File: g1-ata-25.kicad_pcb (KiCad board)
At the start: 2 copper layers, 29 parts, among them P1 G1_DC_SOCKET, P2 G1_GD_PLUGNH, P3 IDE_40PIN, P4 IDE_44PIN, P5 CONN_01X02, P6 CONN_01X04, P7 BARREL_JACK, P8 CONN_01X05, U1 TCXO_DFAS11, U2 TS30011-M050

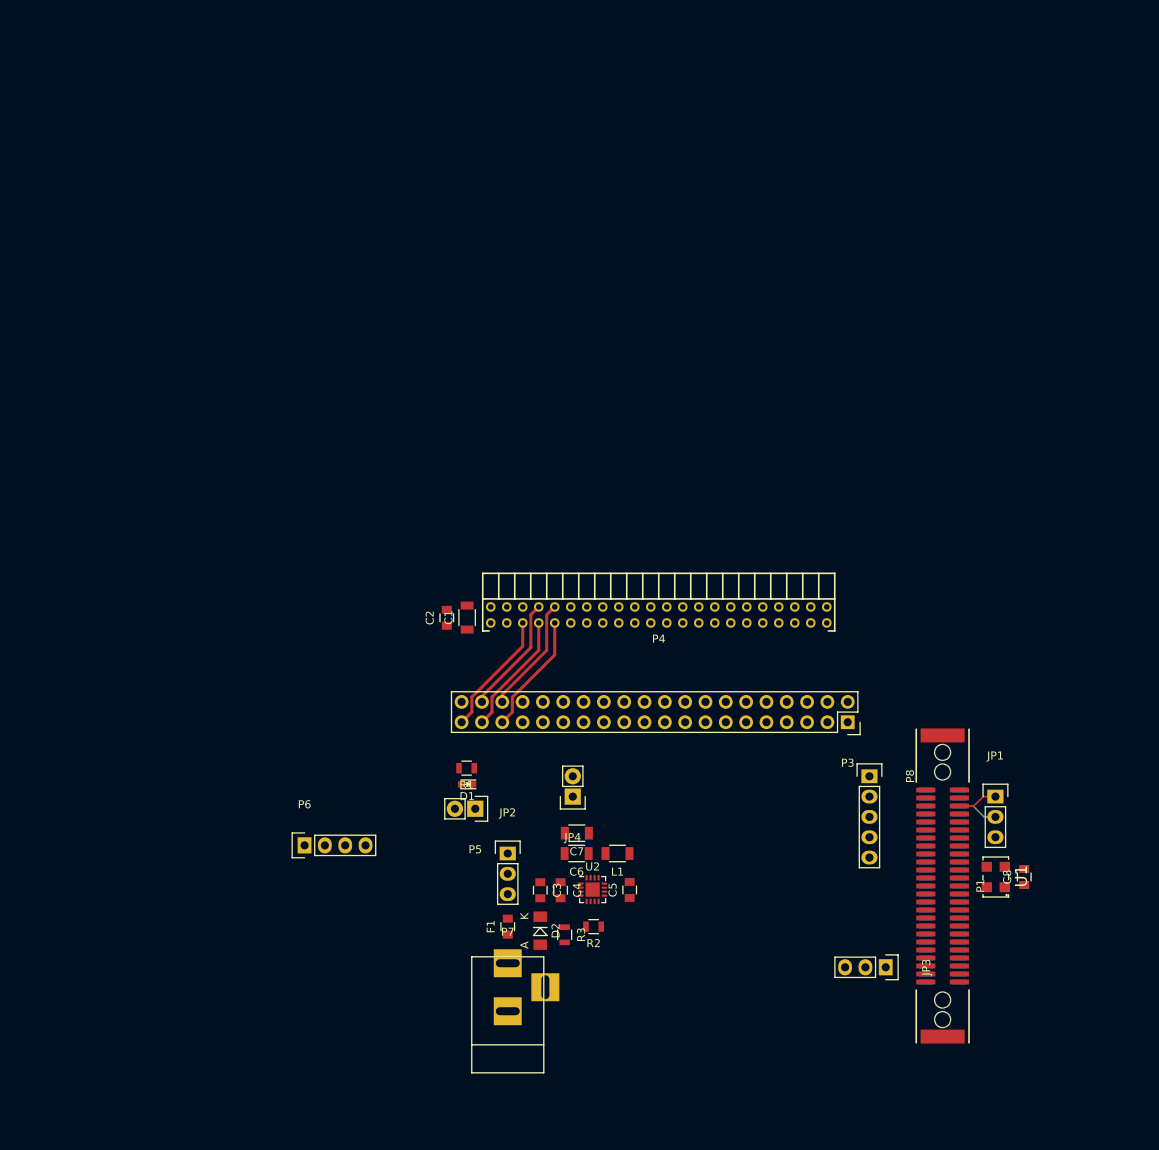
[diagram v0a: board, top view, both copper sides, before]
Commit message: Moved some components.
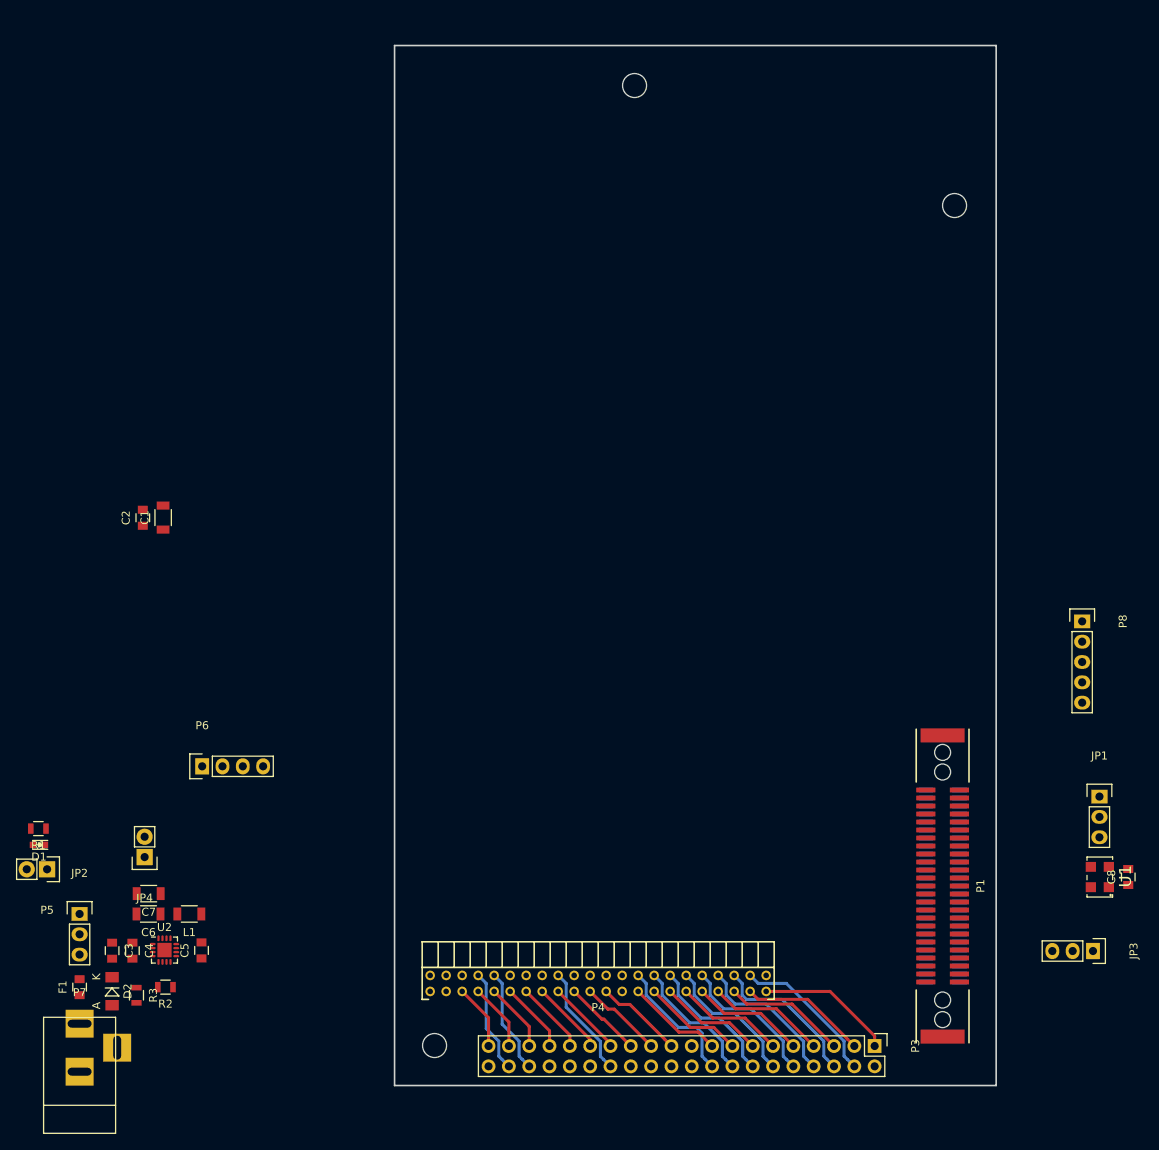
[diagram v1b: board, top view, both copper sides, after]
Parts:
- added MountingHole_3mm: VAL**, Mounting_Holes:MountingHole_3mm, F.Cu at (155.6, 24.4)
- added MountingHole_3mm: VAL**, Mounting_Holes:MountingHole_3mm, F.Cu at (195.6, 39.4)
- added MountingHole_3mm: VAL**, Mounting_Holes:MountingHole_3mm, F.Cu at (130.6, 144.4)
- P3: footprint Socket_Strips:Socket_Strip_Straight_2x20 -> Pin_Headers:Pin_Header_Straight_2x20
- moved C7 54.1 mm to (94.8, 125.4)
- moved C3 54.1 mm to (90.2, 132.5)
- moved C4 54.1 mm to (92.8, 132.5)
- moved C6 54.1 mm to (94.8, 128.0)
- moved D1 54.1 mm to (81.1, 119.3)
- moved D2 54.1 mm to (90.2, 137.6)
- moved JP4 54.1 mm to (94.3, 120.8)
- moved R1 54.1 mm to (81.0, 117.3)
- moved R3 54.1 mm to (93.3, 138.1)
- moved U2 54.1 mm to (96.8, 132.5)
- moved C5 54.1 mm to (101.4, 132.5)
- moved F1 54.1 mm to (86.2, 137.1)
- moved JP2 54.1 mm to (86.2, 128.0)
- moved L1 54.1 mm to (99.9, 128.0)
- moved P5 54.1 mm to (82.1, 122.4)
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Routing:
- net /DD9: track 0.00 -> 19.1 mm
- net /DD8: track 0.00 -> 18.8 mm
- net /DD10: track 0.00 -> 18.6 mm
- net /DD11: track 0.00 -> 18.1 mm
- net /DD12: track 0.00 -> 17.5 mm
- net /~GDD_RST: track 0.00 -> 17.1 mm
- net /DD13: track 0.00 -> 17.0 mm
- net /DD15: track 0.00 -> 16.5 mm
- net /DD14: track 0.00 -> 16.4 mm
- net /DD7: track 0.00 -> 15.8 mm
- net /DD6: track 0.00 -> 15.3 mm
- net /DD5: track 0.00 -> 14.8 mm
- net /DD4: track 0.00 -> 14.2 mm
- net /CSEL: track 0.00 -> 14.1 mm
- net /DD3: track 0.00 -> 13.7 mm
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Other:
- board outline added: 75.2 x 130 mm
- board text added: "10.65"
- board text added: "6.7"

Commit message: Routing...
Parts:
- P7: value BARREL_JACK -> CONN_01X02; footprint Connect:BARREL_JACK -> Sockets_WAGO734:WAGO_734_2pin_Straight_RuggedPads
- moved R3 153.6 mm to (194.3, 22.4), turned to 0 degrees
- moved C3 151.0 mm to (197.9, 26.7), turned to 90 degrees
- moved R2 148.4 mm to (191.0, 22.4), turned to 0 degrees
- moved C4 147.6 mm to (195.6, 26.7), turned to 90 degrees
- moved U2 141.7 mm to (191.3, 26.8), turned to 180 degrees
- moved P7 140.6 mm to (195.3, 59.2), turned to 270 degrees
- moved F1 138.4 mm to (195.8, 52.6), turned to 0 degrees
- moved C6 138.0 mm to (193.3, 31.4), turned to 0 degrees
- moved D2 137.0 mm to (195.6, 50.0), turned to 180 degrees
- moved C5 135.9 mm to (186.9, 26.9), turned to 270 degrees
- moved C7 134.4 mm to (193.2, 33.9), turned to 0 degrees
- moved JP2 134.2 mm to (192.8, 46.5), turned to 90 degrees
- moved L1 130.9 mm to (188.2, 31.4), turned to 0 degrees
- moved JP3 114.9 mm to (182.4, 21.8), turned to 0 degrees
- moved P5 112.1 mm to (134.6, 23.4)
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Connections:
- P8 pad 1: /CD_LRCK -> /~CD_LRCK
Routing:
- net +5V: track 0.00 -> 178.1 mm
- net +5VP: track 0.00 -> 129.4 mm, vias 0 -> 2
- net /CSEL: track 14.1 -> 126.5 mm, vias 0 -> 1
- net /~ACTIVE: track 8.19 -> 117.7 mm
- net /IORDY: track 9.53 -> 111.4 mm, vias 0 -> 2
- net /INTRQ: track 9.09 -> 109.2 mm, vias 0 -> 2
- net /DA1: track 8.86 -> 107.3 mm, vias 0 -> 2
- net /DA2: track 13.2 -> 107.7 mm, vias 0 -> 2
- net /~IDE_CS1: track 13.0 -> 96.5 mm, vias 0 -> 1
- net +12P: track 0.00 -> 82.8 mm, vias 0 -> 3
- net /~IDE_WR: track 10.5 -> 79.8 mm, vias 0 -> 1
- net /~IDE_CS0: track 8.41 -> 76.5 mm, vias 0 -> 1
- net /DA0: track 8.64 -> 75.1 mm, vias 0 -> 1
- net /~DMACK: track 9.31 -> 67.7 mm, vias 0 -> 1
- net /DD0: track 12.1 -> 68.8 mm, vias 0 -> 1
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- added copper zone on F.Cu, net +12V
- added copper zone on F.Cu, net GND
- added copper zone on F.Cu, net Net-(C5-Pad2)
- added copper zone on F.Cu, net Net-(C6-Pad1)
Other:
- board size 75.2 x 130 mm -> 75.2 x 130.4 mm
- board text added: "- Add holes for HDD screws. - Check oscillator pinout. - Check inductor pinout. - Check fuse pinout."
- board text removed: "Barrel jack for power doesn't make too much sense."

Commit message: Routing almost finished.
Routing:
- net +3V3: track 13.2 -> 74.7 mm, vias 0 -> 3
- net GND: track 3.36 -> 44.2 mm, vias 4 -> 38
- net +12V: track 23.2 -> 43.9 mm, vias 0 -> 5
- net Net-(D2-Pad1): track 2.75 -> 6.52 mm
- net +5V: track 178.1 -> 178.9 mm
- net /DD13: track 65.3 -> 65.9 mm
- added copper zone on B.Cu, net +12V
- added copper zone on B.Cu, net GND
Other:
- board text added: "- Add holes for HDD screws. - Check oscillator pinout. - Check inductor footprint. - Check fuse pinout."
- board text removed: "- Add holes for HDD screws. - Check oscillator pinout. - Check inductor pinout. - Check fuse pinout."

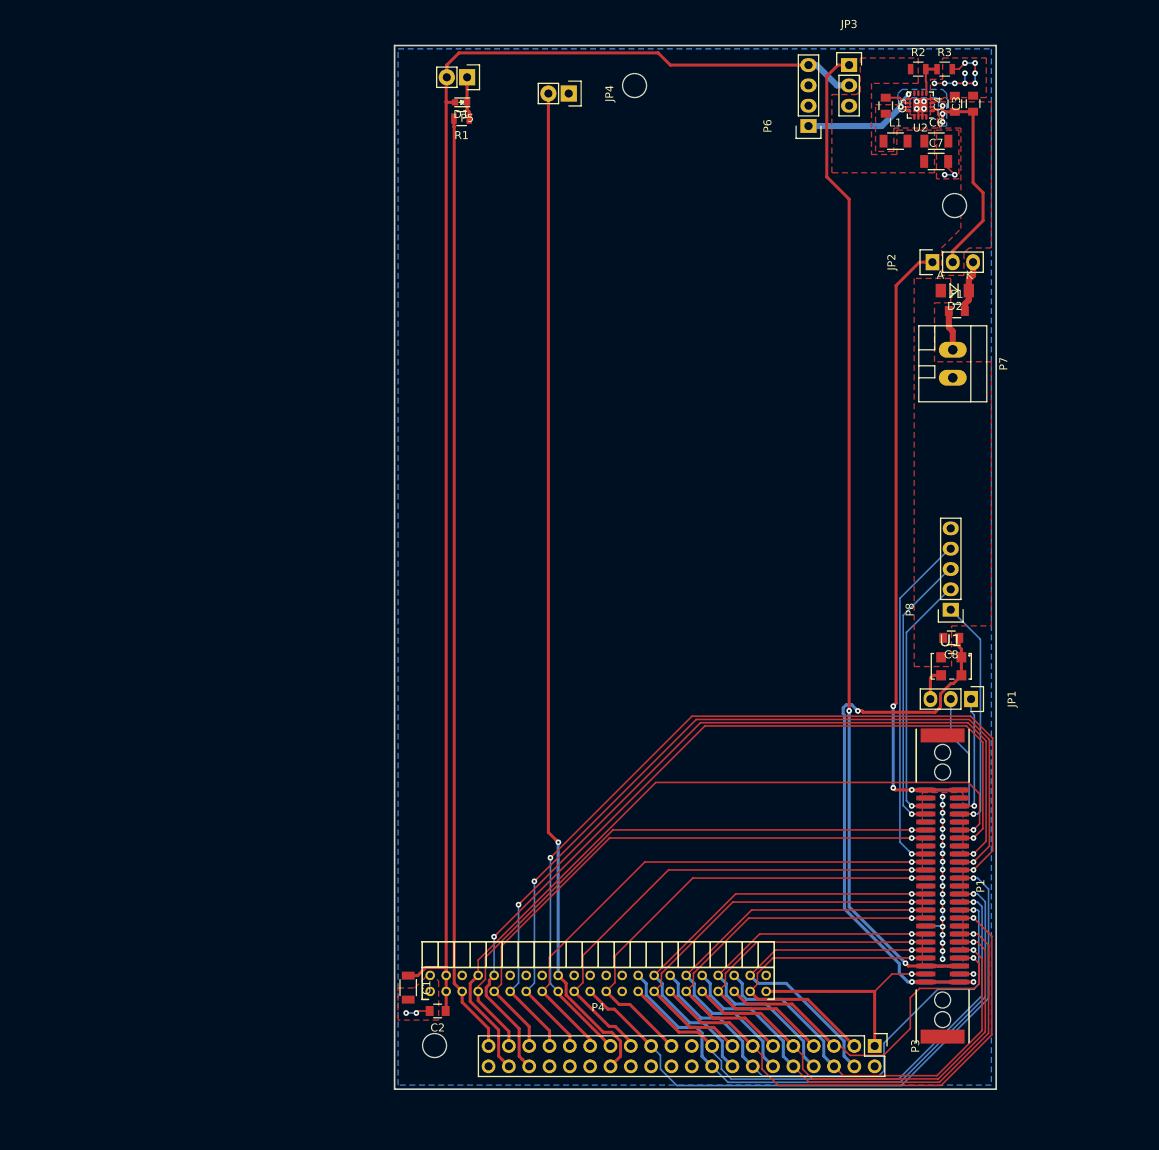
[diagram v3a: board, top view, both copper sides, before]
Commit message: Small routing tweaks to power linea mainly. Also added HDD holes.
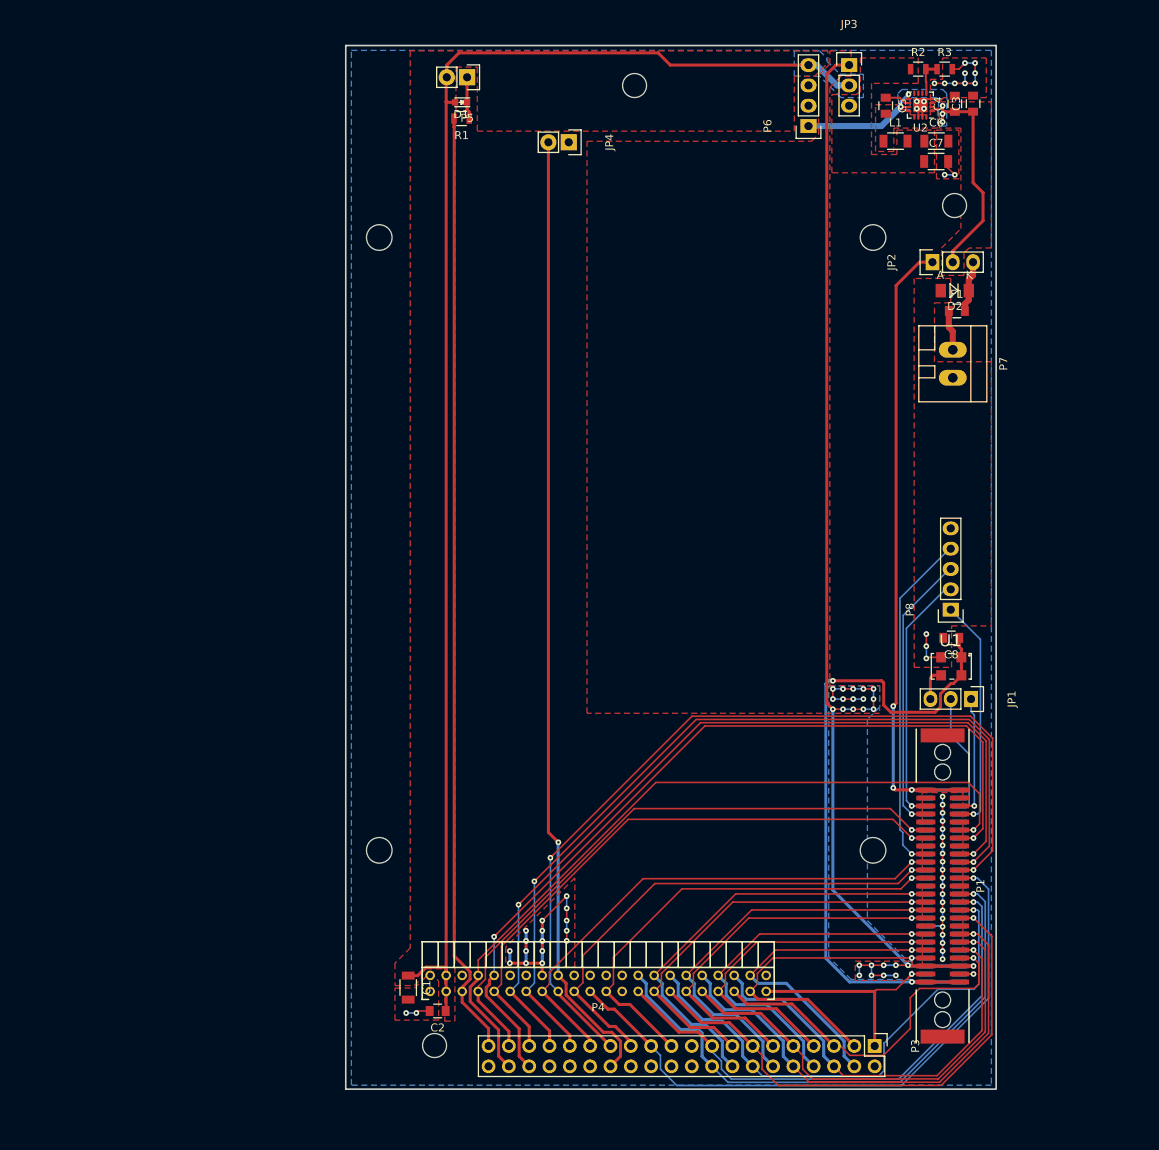
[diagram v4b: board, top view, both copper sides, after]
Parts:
- added REF**: MountingHole_3.2mm_M3_DIN965, Mounting_Holes:MountingHole_3.2mm_M3_DIN965, F.Cu at (185.4, 43.4)
- added REF**: MountingHole_3.2mm_M3_DIN965, Mounting_Holes:MountingHole_3.2mm_M3_DIN965, F.Cu at (123.6, 43.4)
- added REF**: MountingHole_3.2mm_M3_DIN965, Mounting_Holes:MountingHole_3.2mm_M3_DIN965, F.Cu at (185.4, 120.0)
- added REF**: MountingHole_3.2mm_M3_DIN965, Mounting_Holes:MountingHole_3.2mm_M3_DIN965, F.Cu at (123.6, 120.0)
- moved JP4 6.10 mm to (147.3, 31.5)
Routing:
- net +5VP: track 129.4 -> 164.8 mm, vias 2 -> 25
- net GND: track 44.2 -> 75.6 mm, vias 38 -> 57
- net +3V3: track 74.7 -> 86.2 mm, vias 3 -> 2
- net /CSEL: track 126.5 -> 120.4 mm
- net /~IDE_CS0: track 76.5 -> 78.7 mm
- net /DA0: track 75.1 -> 77.0 mm
- net /~DMACK: track 67.7 -> 66.6 mm
- net /~ACTIVE: track 117.7 -> 118.5 mm
- added copper zone on B.Cu, net +5V
- added copper zone on F.Cu, net +5V
- added copper zone on B.Cu, net +5VP
- added copper zone on F.Cu, net +5VP
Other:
- board size 75.2 x 130.4 mm -> 81.3 x 130.4 mm
- board text added: "- Check oscillator pinout. - Check inductor footprint. - Check fuse pinout."
- board text removed: "- Add holes for HDD screws. - Check oscillator pinout. - Check inductor footprint. - Check fuse pinout."

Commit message: Added an external 5V power source plus other tweaks.
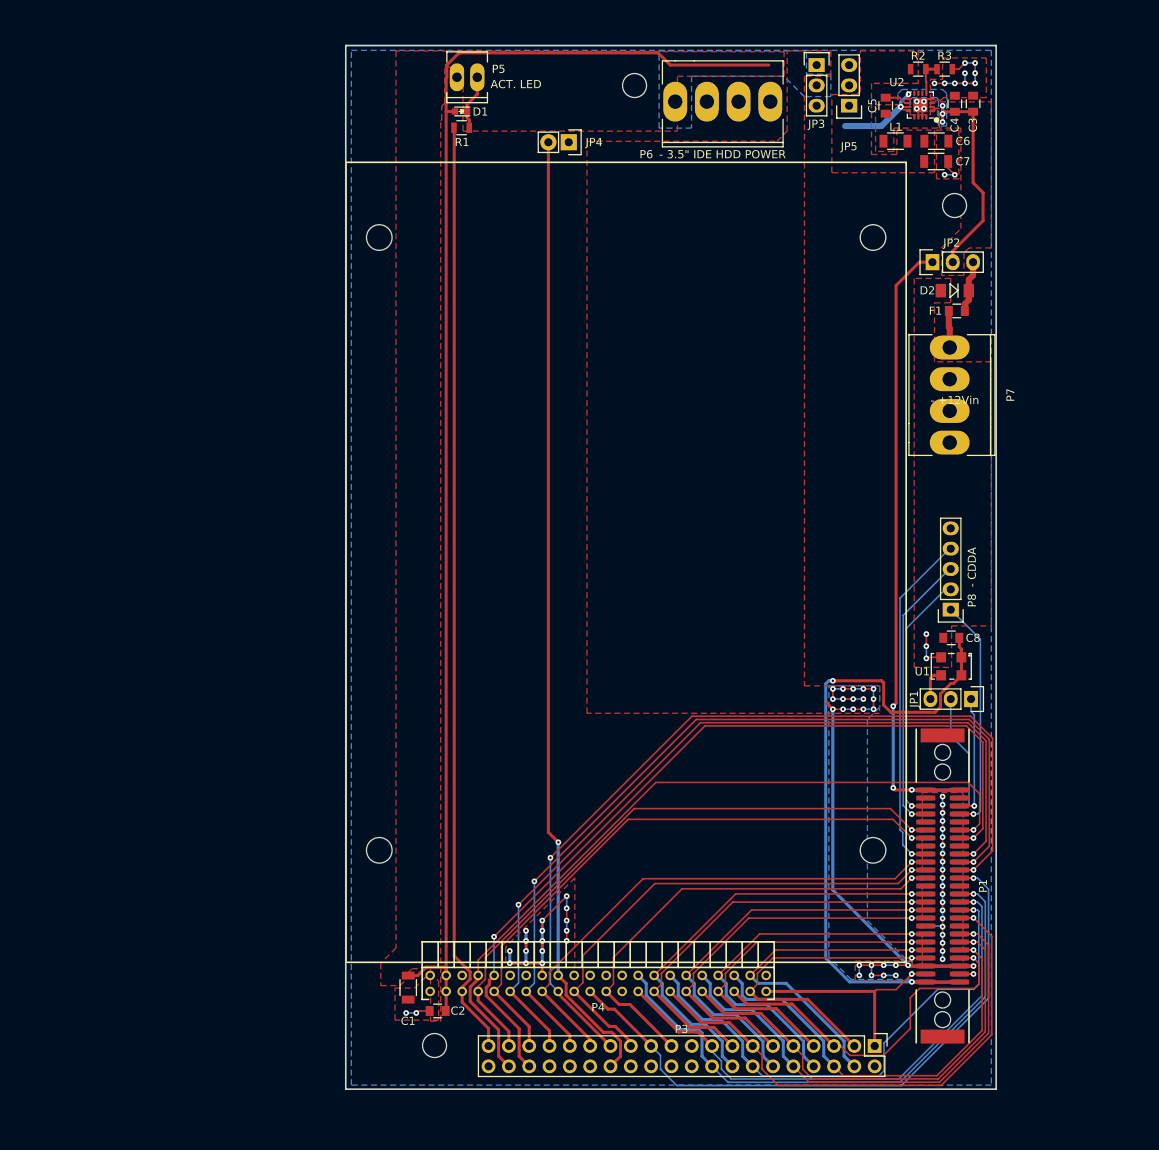
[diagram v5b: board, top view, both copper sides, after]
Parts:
- added JP5: JUMPER3, Pin_Headers:Pin_Header_Straight_1x03, F.Cu at (182.4, 26.9)
- P5: footprint Socket_Strips:Socket_Strip_Straight_1x02 -> Sockets_MOLEX_KK-System:Socket_MOLEX-KK-RM2-54mm_Lock_2pin_straight
- P6: footprint Socket_Strips:Socket_Strip_Straight_1x04 -> Sockets_MOLEX_KK-System:Socket_MOLEX-KK-RM3-96mm_Lock_4pin_straight
- P7: value CONN_01X02 -> CONN_01X04; footprint Sockets_WAGO734:WAGO_734_2pin_Straight_RuggedPads -> Sockets_MOLEX_KK-System:Socket_MOLEX-KK-RM3-96mm_Lock_4pin_straight
- moved P6 11.1 mm to (166.6, 26.4), turned to 180 degrees
- moved JP3 4.06 mm to (178.3, 21.8)
- moved P7 3.93 mm to (194.9, 63.1)
- moved D1 1.14 mm to (133.9, 27.6)
- moved R1 1.14 mm to (133.9, 29.7)
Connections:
- JP3 pad 3: Net-(C6-Pad1) -> Net-(JP3-Pad3)
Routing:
- net +5VP: track 164.8 -> 82.9 mm
- net +5V: track 178.9 -> 167.7 mm
- net +12V: track 43.9 -> 39.4 mm
- net Net-(D1-Pad1): track 5.28 -> 7.01 mm
- net /~ACTIVE: track 118.5 -> 117.4 mm
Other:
- outline, holes or cut-outs redrawn
- board text added: "- +12Vin"
- board text added: "- 3.5" IDE HDD POWER"
- board text added: "- CDDA"
- board text added: "ACT. LED"
- board text removed: "10.65"
- board text removed: "6.7"
